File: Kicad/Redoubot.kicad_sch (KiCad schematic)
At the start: 11 parts, among them U1 STM32G431RBTx, U3 LD39050PU33R, Y1 8MHz

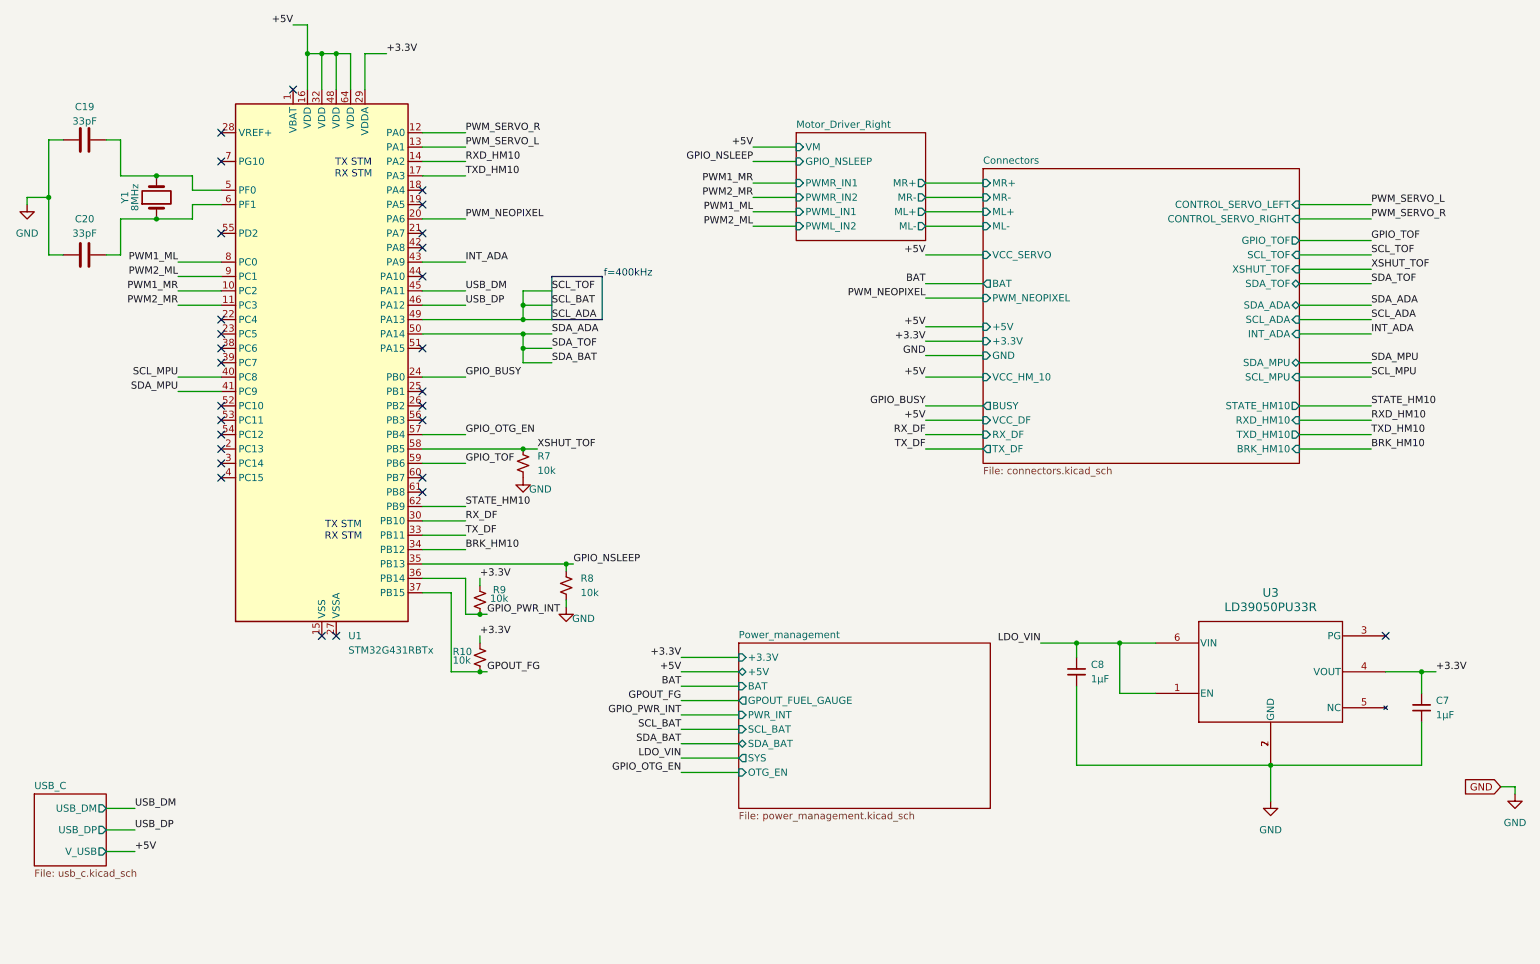
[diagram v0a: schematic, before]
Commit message: Feat: Added power LEDs 5v and 3v, Added Jumpers to battery and bms, Added segmentation in connector sheet, Added encoders, Changed page name from motor diver right to motor driver, Redid annotations, Changed output organisation on stm to match new ioc
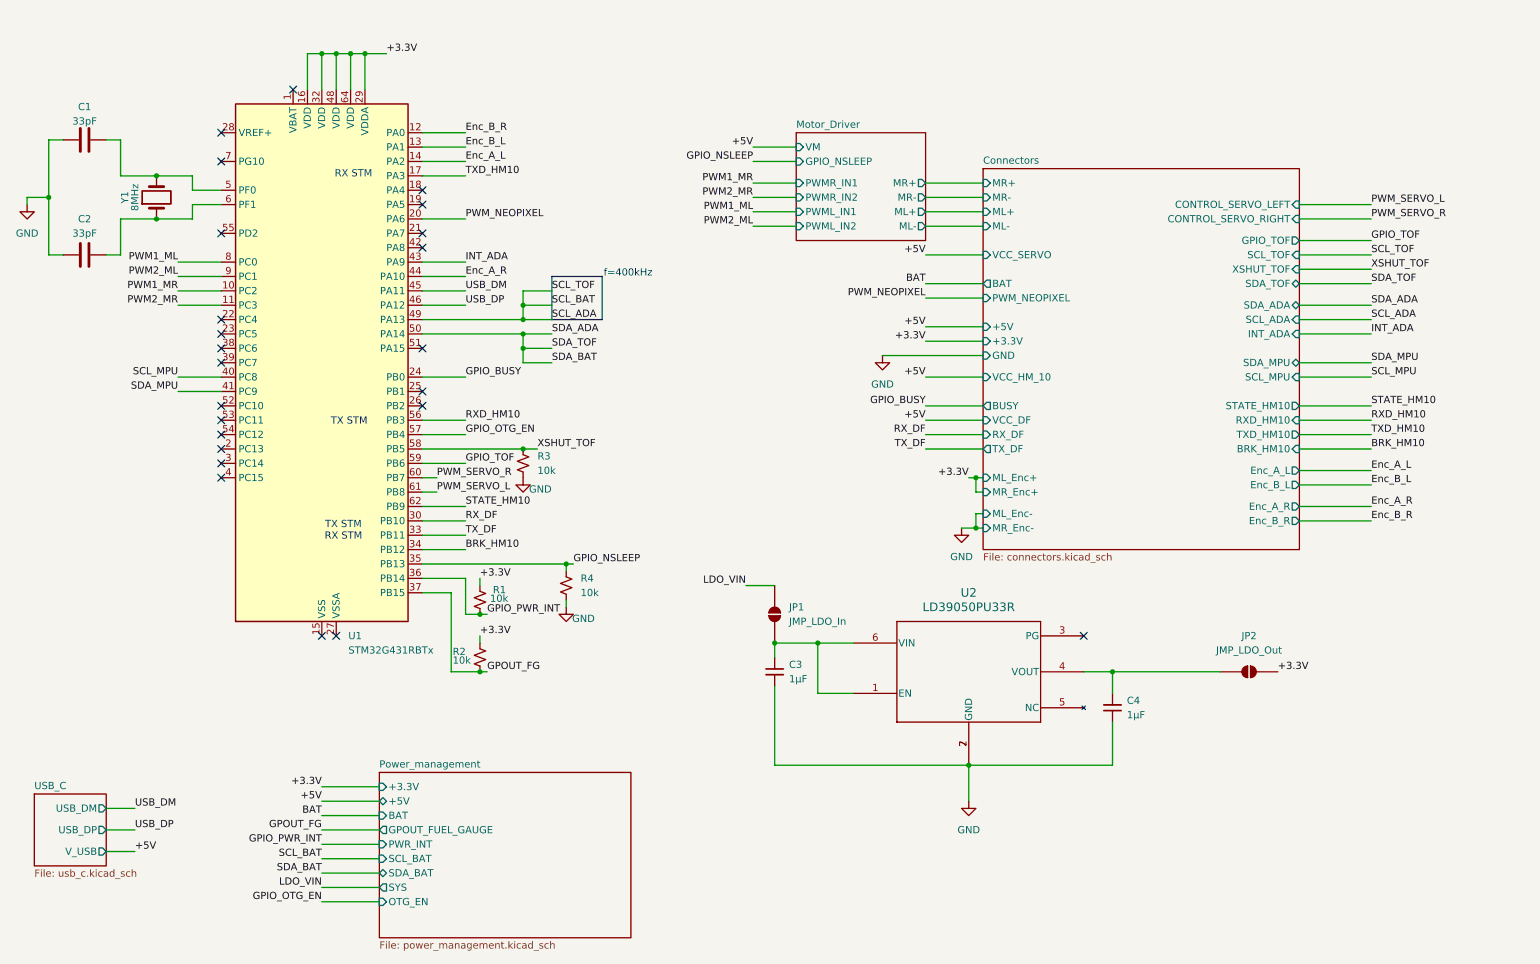
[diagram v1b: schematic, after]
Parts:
- added JP1: JMP_LDO_In, symbol Jumper:SolderJumper_2_Open
- added JP2: JMP_LDO_Out, symbol Jumper:SolderJumper_2_Open
- renumbered C19 to C1, C20 to C2, C8 to C3, C7 to C4, R9 to R1, R10 to R2, R7 to R3, R8 to R4, U3 to U2
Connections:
- net +3.3V: now also U1.16 (VDD), U1.32 (VDD), U1.48 (VDD), U1.64 (VDD), JP2.2 (B); no longer C4.1, U2.4 (VOUT)
- net +5V: no longer U1.16 (VDD), U1.32 (VDD), U1.48 (VDD), U1.64 (VDD)
- net LDO_VIN: now also JP1.2 (B); no longer C3.1, U2.1 (EN), U2.6 (VIN)
- net PWM_SERVO_L: now also U1.61 (PB8); no longer U1.13 (PA1)
- net PWM_SERVO_R: now also U1.60 (PB7); no longer U1.12 (PA0)
- net RXD_HM10: now also U1.56 (PB3); no longer U1.14 (PA2)
- net Enc_A_R: now reaches U1.44 (PA10)
- new net: C4.1, JP2.1 (A), U2.4 (VOUT)
- new net: C3.1, JP1.1 (A), U2.1 (EN), U2.6 (VIN)
- new net Enc_A_L: U1.14 (PA2)
- new net Enc_B_L: U1.13 (PA1)
- new net Enc_B_R: U1.12 (PA0)
- no-connect marks 28 -> 24
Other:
- sheet Motor_Driver_Right renamed Motor_Driver
- sheet Connectors ports: added Enc_A_L, Enc_A_R, Enc_B_L, Enc_B_R, ML_Enc+, ML_Enc-, MR_Enc+, MR_Enc-; removed none
- note added: "RX STM"
- note added: "TX STM"
- moved on the sheet: C3, C4, U2

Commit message: feat: added the footprints for the solderjumpers
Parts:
- JP1, JP2: footprint (none) -> Jumper:SolderJumper-2_P1.3mm_Open_TrianglePad1.0x1.5mm
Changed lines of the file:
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@@
 			)
 		)
-		(property "Footprint" ""
+		(property "Footprint" "Jumper:SolderJumper-2_P1.3mm_Open_TrianglePad1.0x1.5mm"
 			(at 232.41 133.35 0)
 			(hide yes)
@@
 			)
 		)
-		(property "Footprint" ""
+		(property "Footprint" "Jumper:SolderJumper-2_P1.3mm_Open_TrianglePad1.0x1.5mm"
 			(at 148.59 123.19 0)
 			(hide yes)

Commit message: feat: added power flags, no errors during ERC
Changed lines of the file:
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@@
 	)
 	(junction
+		(at 16.51 49.53)
+		(diameter 0)
+		(color 0 0 0 0)
+	)
+	(junction
 		(at 96.52 123.19)
 		(diameter 0)
@@
 	)
 	(junction
+		(at 66.04 24.13)
+		(diameter 0)
+		(color 0 0 0 0)
+	)
+	(junction
 		(at 184.15 107.95)
 		(diameter 0)
@@
 	)
 	(symbol
+		(lib_id "power:PWR_FLAG")
+		(at 66.04 24.13 0)
+		(unit 1)
+		(body_style 1)
+		(exclude_from_sim no)
+		(in_bom yes)
+		(on_board yes)
+		(in_pos_files yes)
+		(dnp no)
+		(property "Reference" "#FLG02"
+			(at 66.04 22.225 0)
+			(hide yes)
+			(show_name no)
+			(do_not_autoplace no)
+			(effects
+				(font
+					(size 1.27 1.27)
+				)
+			)
+		)
+		(property "Value" "PWR_FLAG"
+			(at 66.04 20.828 0)
+			(show_name no)
+			(do_not_autoplace no)
+			(effects
+				(font
+					(size 0.635 0.635)
+				)
+			)
+		)
+		(property "Footprint" ""
+			(at 66.04 24.13 0)
+			(hide yes)
+			(show_name no)
+			(do_not_autoplace no)
+			(effects
+				(font
+					(size 1.27 1.27)
+				)
+			)
+		)
+		(property "Datasheet" ""
+			(at 66.04 24.13 0)
+			(hide yes)
+			(show_name no)
+			(do_not_autoplace no)
+			(effects
+				(font
+					(size 1.27 1.27)
+				)
+			)
+		)
+		(property "Description" "Special symbol for telling ERC where power comes from"
+			(at 66.04 24.13 0)
+			(hide yes)
+			(show_name no)
+			(do_not_autoplace no)
+			(effects
+				(font
+					(size 1.27 1.27)
+				)
+			)
+		)
+		(pin "1"
+		)
+		(instances
+			(project "Redoubot"
+				(path "/43131b41-4104-4cd6-9c2f-4d5da1687300"
+					(reference "#FLG02")
+					(unit 1)
+				)
+			)
+		)
+	)
+	(symbol
 		(lib_id "power:GND")
 		(at 181.61 107.95 0)
@@
 					(unit 1)
 				)
+			)
+		)
+	)
+	(symbol
+		(lib_id "power:PWR_FLAG")
+		(at 16.51 49.53 0)
+		(unit 1)
+		(body_style 1)
+		(exclude_from_sim no)
+		(in_bom yes)
+		(on_board yes)
+		(in_pos_files yes)
+		(dnp no)
+		(property "Reference" "#FLG01"
+			(at 16.51 47.625 0)
+			(hide yes)
+			(show_name no)
+			(do_not_autoplace no)
+			(effects
+				(font
+					(size 1.27 1.27)
+				)
+			)
+		)
+		(property "Value" "PWR_FLAG"
+			(at 16.51 46.482 0)
+			(show_name no)
+			(do_not_autoplace no)
+			(effects
+				(font
+					(size 0.635 0.635)
+				)
+			)
+		)
+		(property "Footprint" ""
+			(at 16.51 49.53 0)
+			(hide yes)
+			(show_name no)
+			(do_not_autoplace no)
+			(effects
+				(font
+					(size 1.27 1.27)
+				)
+			)
+		)
+		(property "Datasheet" ""
+			(at 16.51 49.53 0)
+			(hide yes)
+			(show_name no)
+			(do_not_autoplace no)
+			(effects
+				(font
+					(size 1.27 1.27)
+				)
+			)
+		)
+		(property "Description" "Special symbol for telling ERC where power comes from"
+			(at 16.51 49.53 0)
+			(hide yes)
+			(show_name no)
+			(do_not_autoplace no)
+			(effects
+				(font
+					(size 1.27 1.27)
+				)
+			)
+		)
+		(pin "1"
+		)
+		(instances
+			(project "Redoubot"
+				(path "/43131b41-4104-4cd6-9c2f-4d5da1687300"
+					(reference "#FLG01")
+					(unit 1)
+				)

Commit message: feat: electrical schematic validated
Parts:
- removed C1, C2: 33pF, Capacitor_SMD:C_0402_1005Metric, symbol Device:C
- removed C3, C4: 1µF, Capacitor_SMD:C_0402_1005Metric, symbol Device:C_Small
- removed JP1: JMP_LDO_In, Jumper:SolderJumper-2_P1.3mm_Open_TrianglePad1.0x1.5mm, symbol Jumper:SolderJumper_2_Open
- removed JP2: JMP_LDO_Out, Jumper:SolderJumper-2_P1.3mm_Open_TrianglePad1.0x1.5mm, symbol Jumper:SolderJumper_2_Open
- removed R1, R2, R3, R4: 10k, Resistor_SMD:R_0402_1005Metric, symbol Device:R_Small_US
- removed U1: STM32G431RBTx, Package_QFP:LQFP-64_10x10mm_P0.5mm, symbol MCU_ST_STM32G4:STM32G431RBTx
- removed U2: LD39050PU33R, footprints_LD39:DFN6_3X3_STM, symbol LD39050PU33R:LD39050PU33R
- removed Y1: 8MHz, Crystal:Crystal_SMD_HC49-SD, symbol Device:Crystal
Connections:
- no-connect marks 24 -> 0
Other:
- sheet Connectors renamed Sensors
- removed sheet USB_C
- added sheet STM32 (stm32.kicad_sch)
- sheet Motor_Driver ports: added none; removed VM
- sheet Power_management ports: added USB_DM, USB_DP; removed +3.3V, +5V, BAT, OTG_EN, SYS
- sheet Sensors ports: added none; removed +3.3V, +5V, BAT, GND, ML_Enc+, ML_Enc-, MR_Enc+, MR_Enc-, VCC_DF, VCC_HM_10, VCC_SERVO
- note removed: "RX STM"
- note removed: "TX STM"
- note removed: "TX STM RX STM"
- note removed: "f=400kHz"

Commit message: Feat: Placed components on wiring schematic, chore: fixed footprint names and values
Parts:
- added H1, H2, H3, H4: MountingHole_Pad, MountingHole:MountingHole_2.2mm_M2_Pad_TopBottom, symbol Mechanical:MountingHole_Pad
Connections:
- new net GND: H1.1, H2.1, H3.1, H4.1
